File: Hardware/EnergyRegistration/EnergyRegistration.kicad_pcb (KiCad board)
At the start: 2 copper layers, 28 parts, among them J1 Screw_Terminal_01x04, J2 Screw_Terminal_01x04, J3 Conn_01x06_Male, J4 Screw_Terminal_01x04, Q1 S8550_SOT23, Q2 S8050_SOT23, Q3 S8050_SOT23, U1 L78S05CV

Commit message: Library update
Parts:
- removed J3: Conn_01x06_Male, Local_Connectors:PinHeader_1x06_P2.50mm_Vertical
- removed U1: L78S05CV, Package_TO_SOT_THT:TO-220-3_Vertical
- moved D4 74.8 mm to (157.5, 93.0)
- moved Q1 65.6 mm to (157.9, 89.3)
- moved D2 59.9 mm to (195.3, 55.8)
- moved D9 57.3 mm to (211.9, 35.1)
- moved D1 55.9 mm to (190.8, 58.9)
- moved C2 48.5 mm to (204.8, 43.8)
- moved D11 44.6 mm to (190.6, 44.4)
- moved C1 43.3 mm to (190.9, 55.9)
- moved A1 42.9 mm to (152.4, 35.6)
- moved R4 38.0 mm to (199.8, 52.3)
- moved D7 35.4 mm to (195.7, 52.5)
- moved D3 33.9 mm to (204.7, 46.8)
- moved R2 29.4 mm to (162.3, 91.3)
- moved R6 27.3 mm to (212.4, 39.4)
- moved J1 26.0 mm to (115.5, 92.3)
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
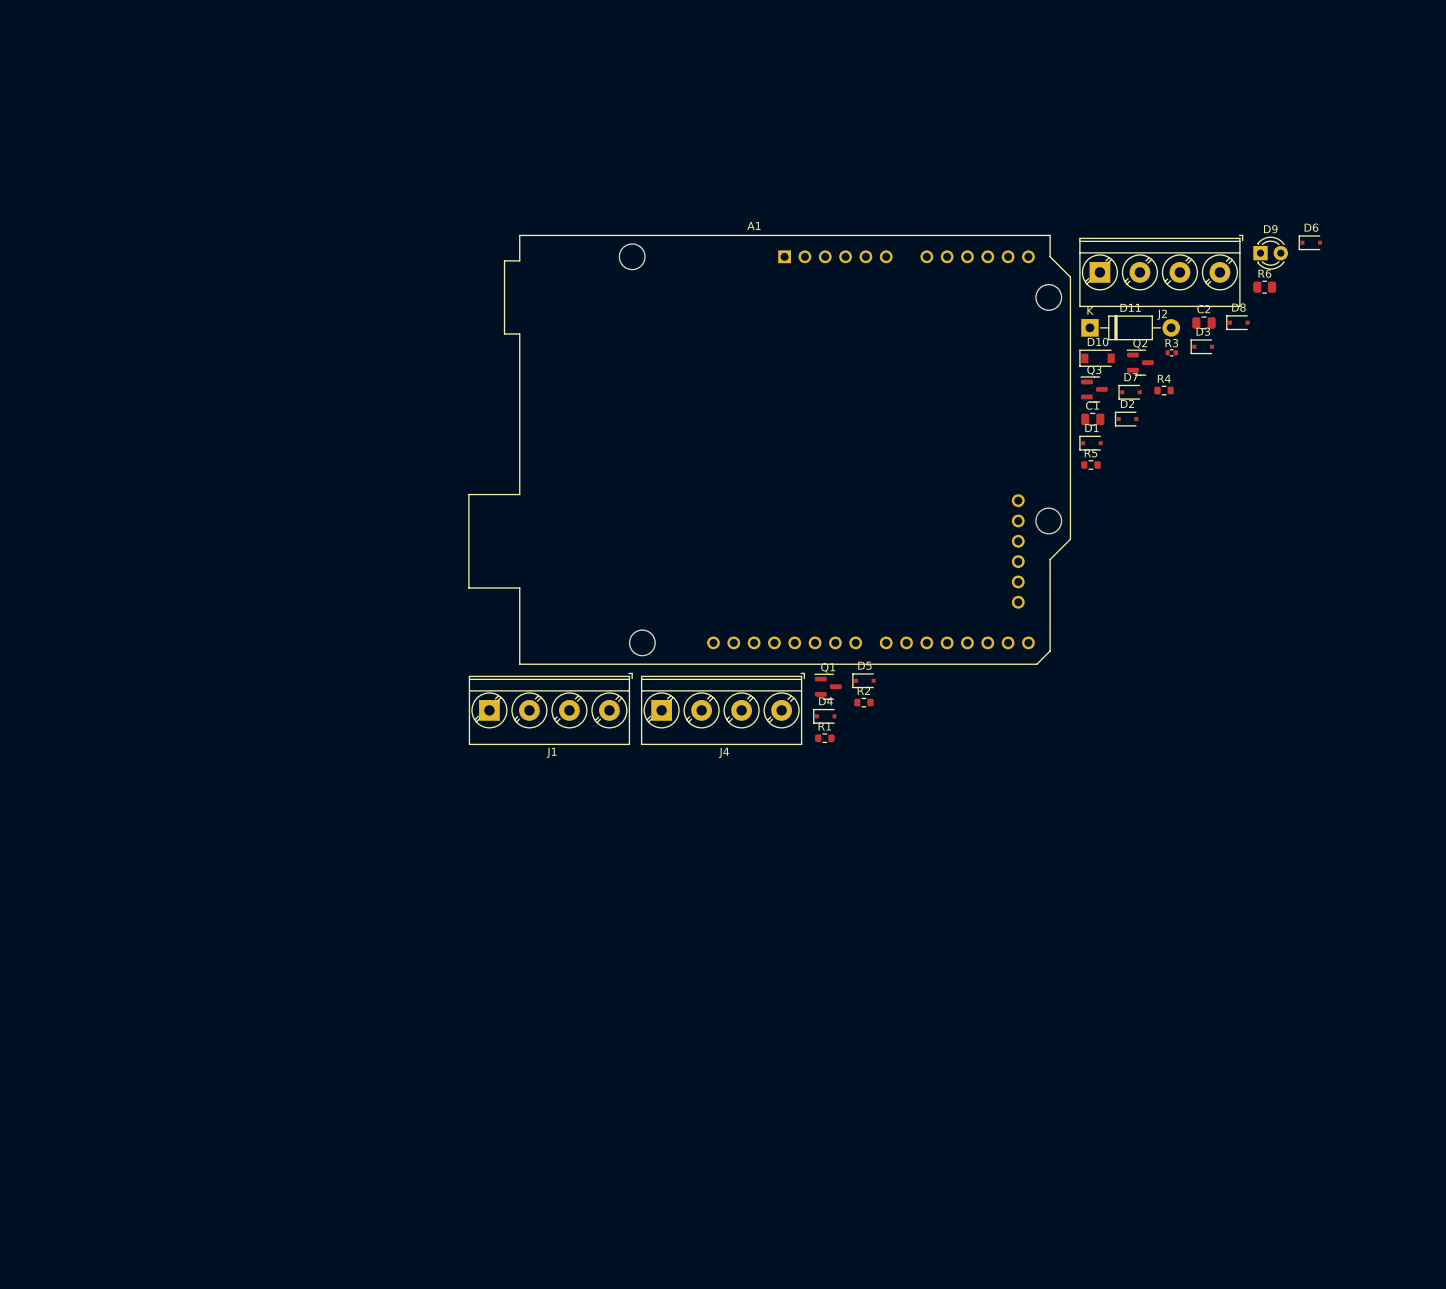
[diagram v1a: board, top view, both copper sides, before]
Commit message: Components changed to SMD
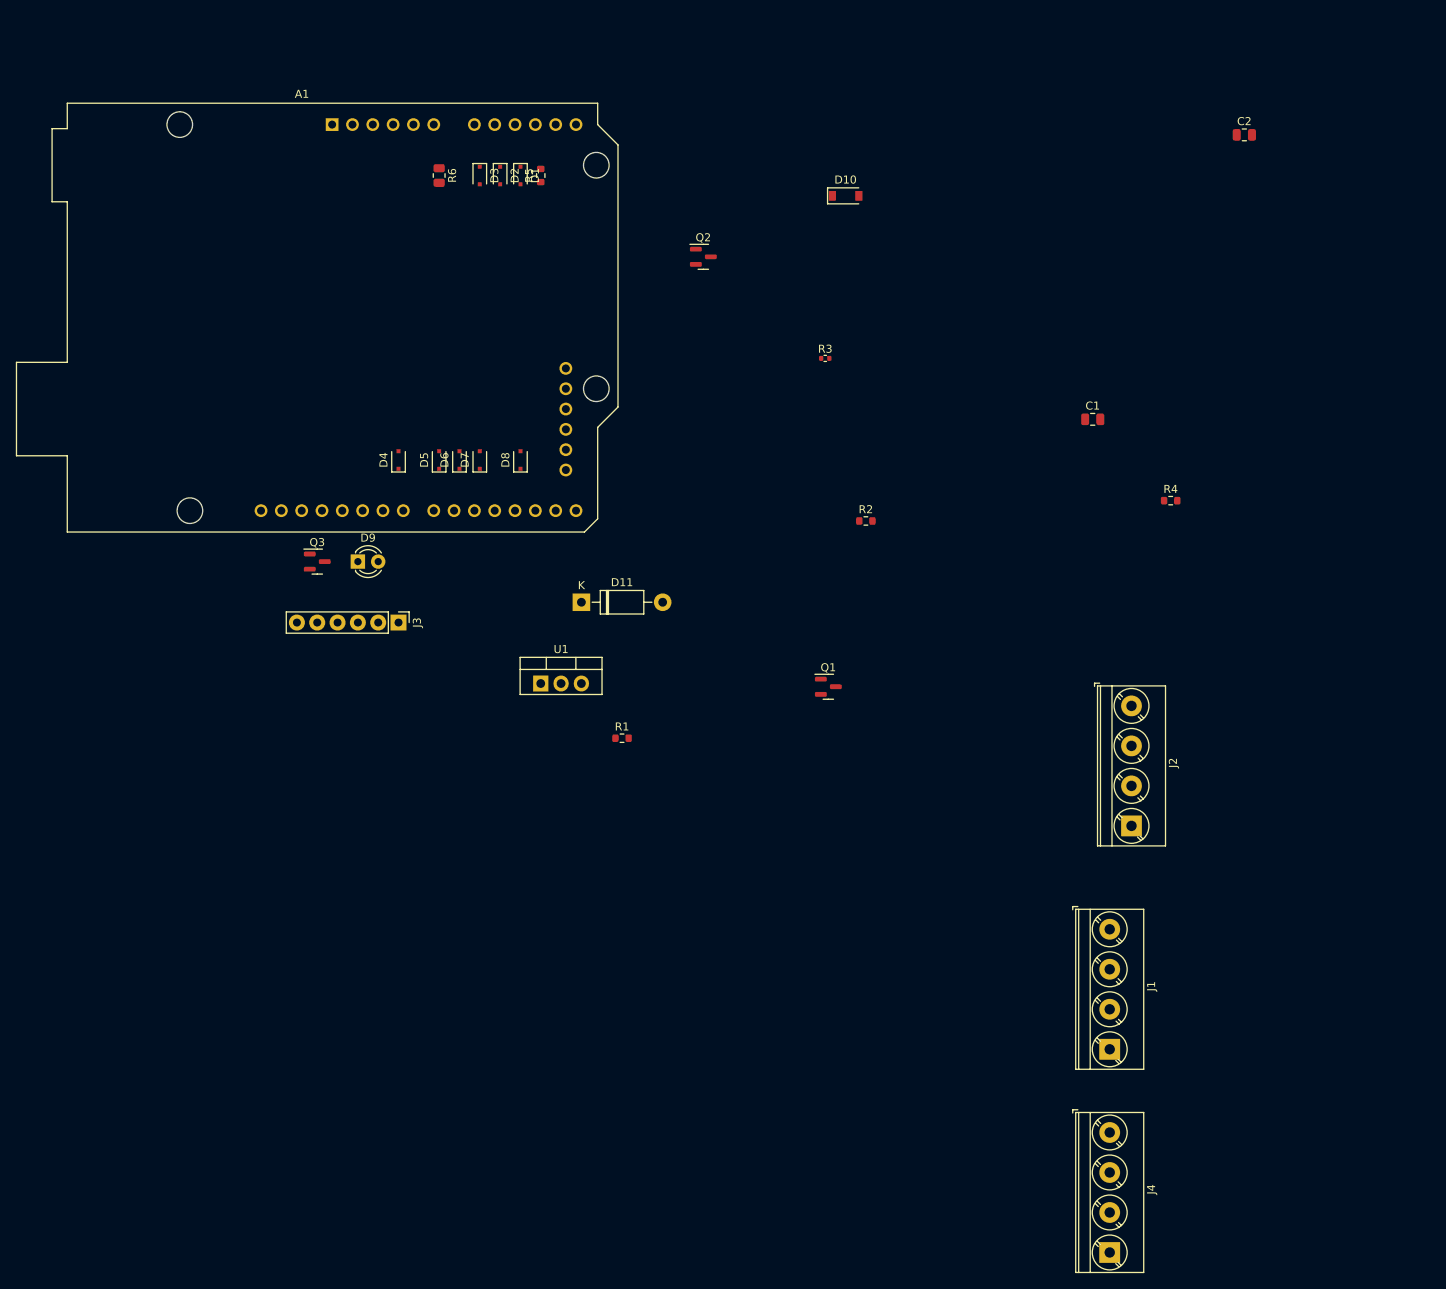
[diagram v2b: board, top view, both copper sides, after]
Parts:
- added J3: Conn_01x06_Male, Local_Connectors:PinHeader_1x06_P_0,1in_Vertical, F.Cu at (104.1, 81.3)
- added U1: L78S05CV, Package_TO_SOT_THT:TO-220-3_Vertical, F.Cu at (121.9, 88.9)
- moved D9 119.2 mm to (99.1, 73.7)
- moved D6 109.9 mm to (111.8, 61.0), turned to 90 degrees
- moved R6 104.1 mm to (109.2, 25.4), turned to -90 degrees
- moved Q3 99.5 mm to (94.0, 73.7)
- moved D3 92.9 mm to (114.3, 25.4), turned to -90 degrees
- moved D8 91.4 mm to (119.4, 61.0), turned to 90 degrees
- moved J1 88.4 mm to (193.0, 134.6), turned to 90 degrees
- moved J4 87.9 mm to (193.0, 160.0), turned to 90 degrees
- moved D2 84.1 mm to (116.8, 25.4), turned to -90 degrees
- moved D7 81.8 mm to (114.3, 61.0), turned to 90 degrees
- moved D1 78.9 mm to (119.4, 25.4), turned to -90 degrees
- moved R5 77.7 mm to (121.9, 25.4), turned to 90 degrees
- moved D11 72.2 mm to (127.0, 78.7)
- moved J2 69.3 mm to (195.8, 106.7), turned to 90 degrees
- moved D4 62.3 mm to (104.1, 61.0), turned to 90 degrees
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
